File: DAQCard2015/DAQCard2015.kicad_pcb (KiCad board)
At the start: 4 copper layers, 160 x 160 mm, 191 parts, among them CON1 BARREL_JACK, K1 1462042-8, P1 QTH-090-01-F-D-A, P2 QTH-090-01-F-D-A, P3 miniDIL20, P4 LEMO_EPY.00.250.NTN, P5 LEMO_EPY.00.250.NTN, P6 FAN, P7 CONN_02X20_Double, P9 SHV, Q1 MMBT2222A-TP, Q2 SBC817-40LT1G, SW1 DPDT, U1 RJ45x8, U10 AD9219, U11 THS4524IDBTR, U12 AD9219, U13 THS4524IDBTR, U14 AD9219, U15 THS4524IDBTR, U16 AD9219, U17 THS4524IDBTR, U18 AD9219, U19 AD8534, U2 AD5628, U20 LM1086, U21 LT1913, U22 AD5628, U23 AD8534, U24 MCP65R41, U3 THS4524IDBTR, U4 AD9219, U5 THS4524IDBTR, U6 AD9219, U7 THS4524IDBTR, U8 AD9219, U9 THS4524IDBTR

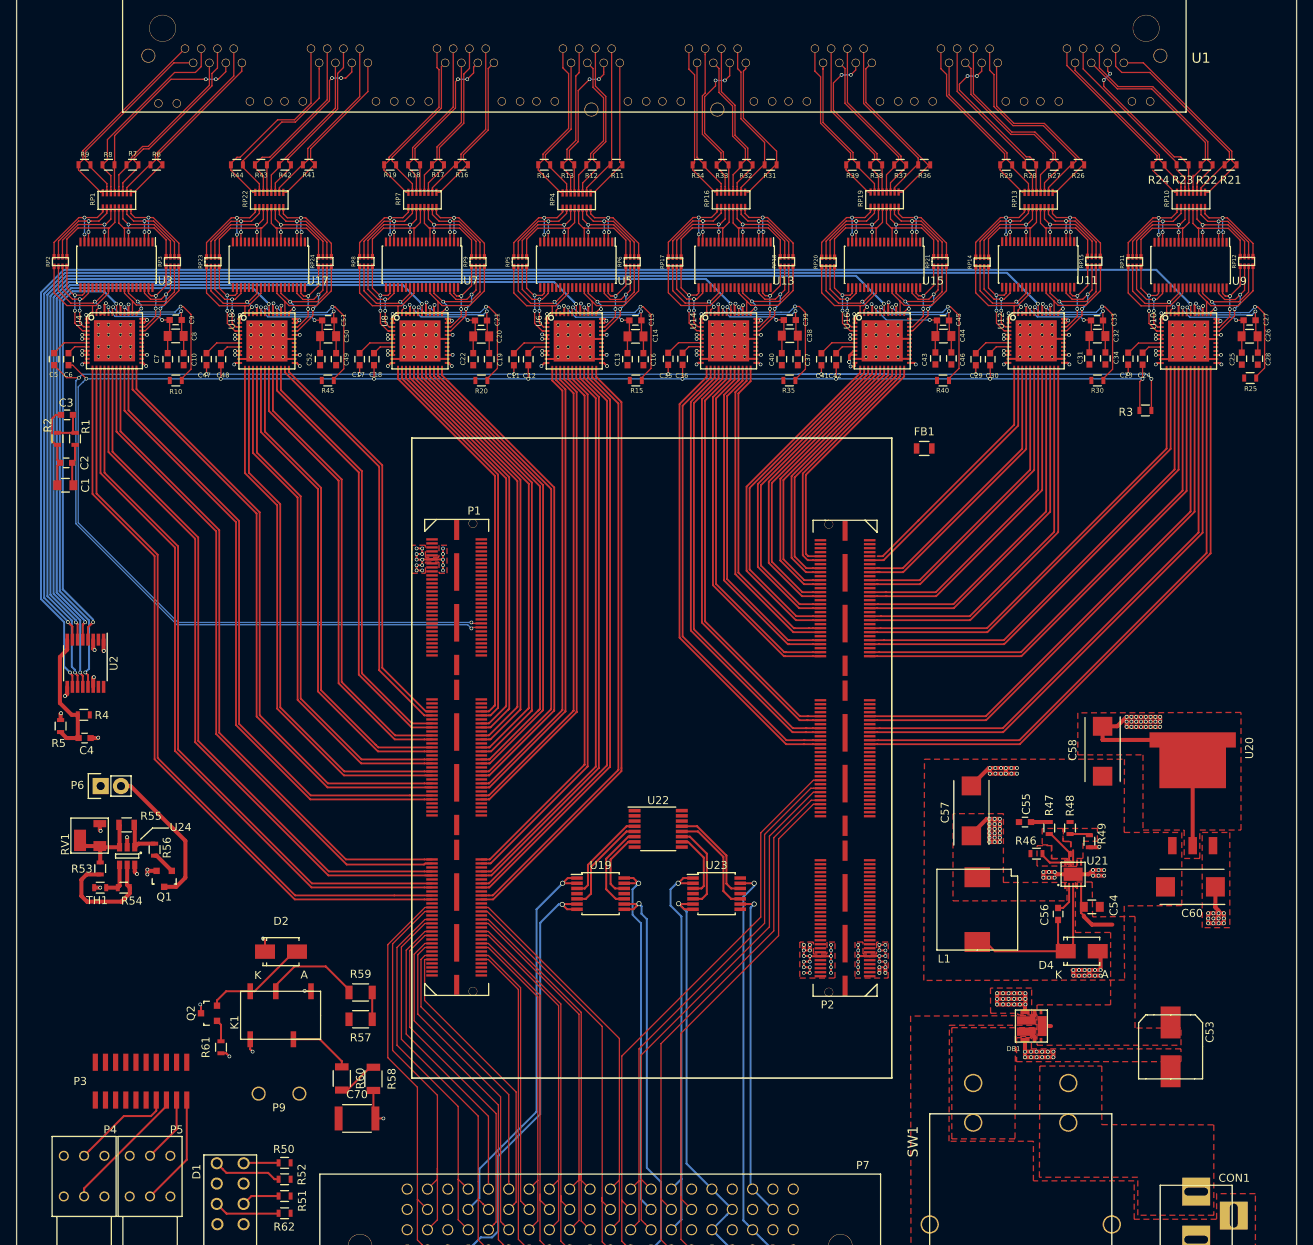
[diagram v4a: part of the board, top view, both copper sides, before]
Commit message: Adds misc traces(gnds, SPI, etc) to DAQ board
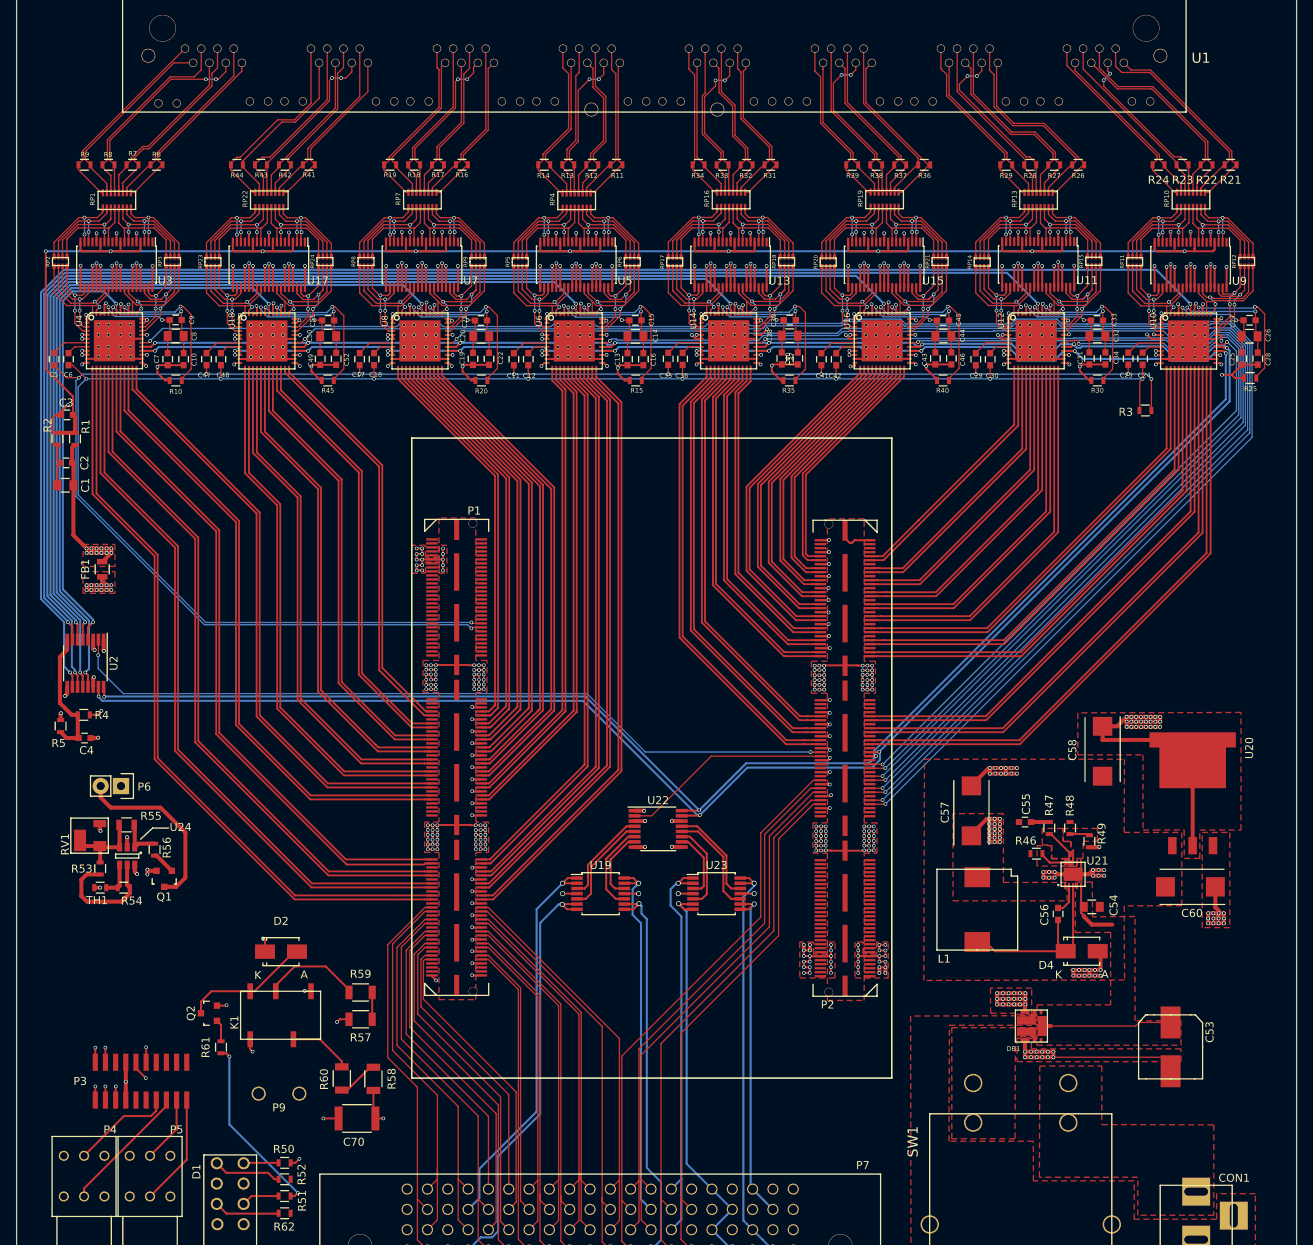
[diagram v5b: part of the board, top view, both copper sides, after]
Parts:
- moved FB1 103.9 mm to (28.7, 96.2), turned to 90 degrees
- moved P6 2.54 mm to (31.1, 123.3), turned to 180 degrees
- moved C19 2.03 mm to (75.0, 69.9)
- moved C52 2.01 mm to (58.0, 69.9)
- moved C37 2.00 mm to (113.7, 69.8)
- moved C40 2.00 mm to (115.7, 69.8)
- moved C49 1.99 mm to (56.0, 69.9)
- moved C22 1.97 mm to (77.0, 69.9)
- moved U13 0.50 mm to (107.2, 58.1)
- turned C20 to 0 degrees
- turned C21 to 180 degrees
- turned C27 to 180 degrees
- turned C38 to 0 degrees
- turned C39 to 180 degrees
- turned C50 to 0 degrees
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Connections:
- P1 pad 102: /ZEM4310/+12VDD -> (no net)
- P1 pad 108: /ZEM4310/+12VDD -> (no net)
- P1 pad 114: /ZEM4310/+12VDD -> (no net)
- P1 pad 115: /ZEM4310/CLKOUT1p -> (no net)
- P1 pad 116: /ZEM4310/CLKIN1p -> (no net)
- P1 pad 117: /ZEM4310/CLKOUT1n -> (no net)
- P1 pad 118: /ZEM4310/CLKIN1n -> (no net)
- P1 pad 120: /ZEM4310/+12VDD -> (no net)
- P1 pad 126: /ZEM4310/+12VDD -> (no net)
- P1 pad 132: /ZEM4310/+12VDD -> (no net)
- P1 pad 138: /ZEM4310/+12VDD -> (no net)
- P1 pad 144: /ZEM4310/+12VDD -> (no net)
- P1 pad 150: /ZEM4310/+12VDD -> (no net)
- P1 pad 156: /ZEM4310/+12VDD -> (no net)
- P1 pad 162: /ZEM4310/+12VDD -> (no net)
- P1 pad 168: /ZEM4310/+12VDD -> (no net)
- P1 pad 174: /ZEM4310/+12VDD -> (no net)
- P1 pad 175: /ZEM4310/CKLOUT2p -> (no net)
- P1 pad 176: /ZEM4310/CLKIN2p -> (no net)
- P1 pad 177: /ZEM4310/CKLOUT2n -> (no net)
- P1 pad 178: /ZEM4310/CLKIN2n -> (no net)
- P1 pad 49: /ZEM4310/HSMC_SDA -> (no net)
- P1 pad 50: /ZEM4310/HSMC_SCL -> (no net)
- P1 pad 51: /ZEM4310/JTAG_TCK -> (no net)
- P1 pad 52: /ZEM4310/JTAG_TMC -> (no net)
- P1 pad 55: /ZEM4310/JTAG_TDO -> (no net)
- P1 pad 56: /ZEM4310/JTAG_TDI -> (no net)
- P1 pad 57: /ZEM4310/CLKOUT0 -> (no net)
- P1 pad 58: /ZEM4310/CLKIN0 -> (no net)
- P1 pad 61: /ZEM4310/D0 -> (no net)
- P1 pad 62: /ZEM4310/D1 -> (no net)
- P1 pad 63: /ZEM4310/D2 -> (no net)
- P1 pad 64: /ZEM4310/D3 -> (no net)
- P1 pad 66: /ZEM4310/+12VDD -> (no net)
- P1 pad 72: /ZEM4310/+12VDD -> (no net)
- P1 pad 78: /ZEM4310/+12VDD -> (no net)
- P1 pad 84: /ZEM4310/+12VDD -> (no net)
- P1 pad 90: /ZEM4310/+12VDD -> (no net)
- P1 pad 96: /ZEM4310/+12VDD -> (no net)
- P2 pad 102: /ZEM4310/+12VDD -> (no net)
- P2 pad 108: /ZEM4310/+12VDD -> (no net)
- P2 pad 114: /ZEM4310/+12VDD -> (no net)
- P2 pad 115: /ZEM4310/CLKOUT1p -> (no net)
- P2 pad 116: /ZEM4310/CLKIN1p -> (no net)
- P2 pad 117: /ZEM4310/CLKOUT1n -> (no net)
- P2 pad 118: /ZEM4310/CLKIN1n -> (no net)
- P2 pad 120: /ZEM4310/+12VDD -> (no net)
- P2 pad 126: /ZEM4310/+12VDD -> (no net)
- P2 pad 132: /ZEM4310/+12VDD -> (no net)
- P2 pad 138: /ZEM4310/+12VDD -> (no net)
- P2 pad 144: /ZEM4310/+12VDD -> (no net)
- P2 pad 150: /ZEM4310/+12VDD -> (no net)
- P2 pad 156: /ZEM4310/+12VDD -> (no net)
- P2 pad 162: /ZEM4310/+12VDD -> (no net)
- P2 pad 168: /ZEM4310/+12VDD -> (no net)
- P2 pad 174: /ZEM4310/+12VDD -> (no net)
- P2 pad 175: /ZEM4310/CKLOUT2p -> (no net)
- P2 pad 176: /ZEM4310/CLKIN2p -> (no net)
- P2 pad 177: /ZEM4310/CKLOUT2n -> (no net)
- P2 pad 178: /ZEM4310/CLKIN2n -> (no net)
- P2 pad 49: /ZEM4310/HSMC_SDA -> (no net)
- P2 pad 50: /ZEM4310/HSMC_SCL -> (no net)
- P2 pad 51: /ZEM4310/JTAG_TCK -> (no net)
- P2 pad 52: /ZEM4310/JTAG_TMC -> (no net)
- P2 pad 55: /ZEM4310/JTAG_TDO -> (no net)
- P2 pad 56: /ZEM4310/JTAG_TDI -> (no net)
- P2 pad 57: /ZEM4310/CLKOUT0 -> (no net)
- P2 pad 58: /ZEM4310/CLKIN0 -> (no net)
- P2 pad 61: /ZEM4310/D0 -> (no net)
- P2 pad 62: /ZEM4310/D1 -> (no net)
- P2 pad 63: /ZEM4310/D2 -> (no net)
- P2 pad 64: /ZEM4310/D3 -> (no net)
- P2 pad 66: /ZEM4310/+12VDD -> (no net)
- P2 pad 68: (no net) -> ADC1_CSB
- P2 pad 70: (no net) -> ADC2_CSB
- P2 pad 72: /ZEM4310/+12VDD -> (no net)
- P2 pad 74: (no net) -> ADC3_CSB
- P2 pad 76: (no net) -> ADC4_CSB
- P2 pad 78: /ZEM4310/+12VDD -> (no net)
- P2 pad 80: (no net) -> ADC5_CSB
- P2 pad 82: (no net) -> ADC6_CSB
- P2 pad 84: /ZEM4310/+12VDD -> (no net)
- P2 pad 86: (no net) -> ADC7_CSB
- P2 pad 88: (no net) -> ADC8_CSB
- P2 pad 90: /ZEM4310/+12VDD -> (no net)
- P2 pad 91: (no net) -> SUPDAC_CSB
- P2 pad 92: (no net) -> SPI_SCLK
- P2 pad 93: (no net) -> RNGDAC_CSB
- P2 pad 94: (no net) -> SPI_SDIO
- P2 pad 96: /ZEM4310/+12VDD -> (no net)
- U10 pad 30: (no net) -> ADC8_CSB
- U12 pad 30: (no net) -> ADC7_CSB
- U14 pad 30: (no net) -> ADC5_CSB
- U16 pad 30: (no net) -> ADC6_CSB
- U18 pad 30: (no net) -> ADC2_CSB
- U2 pad 2: (no net) -> RNGDAC_CSB
- U22 pad 15: (no net) -> SPI_SDIO
- U22 pad 16: (no net) -> SPI_SCLK
- U22 pad 2: (no net) -> SUPDAC_CSB
- U4 pad 30: (no net) -> ADC1_CSB
- U6 pad 30: (no net) -> ADC4_CSB
- U8 pad 30: (no net) -> ADC3_CSB
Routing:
- net GND: track 115.3 -> 509.6 mm, vias 76 -> 324
- net SPI_SDIO: track 0.00 -> 331.6 mm, vias 0 -> 11
- net SPI_SCLK: track 0.00 -> 329.5 mm, vias 0 -> 11
- net Vocm: track 61.8 -> 316.9 mm, vias 1 -> 10
- net ADC1_CSB: track 0.00 -> 222.1 mm, vias 0 -> 2
- net ADC2_CSB: track 0.00 -> 200.4 mm, vias 0 -> 2
- net ADC3_CSB: track 0.00 -> 178.8 mm, vias 0 -> 2
- net ADC4_CSB: track 0.00 -> 158.6 mm, vias 0 -> 2
- net ADC5_CSB: track 0.00 -> 137.1 mm, vias 0 -> 2
- net ADC6_CSB: track 0.00 -> 116.5 mm, vias 0 -> 2
- net RNGDAC_CSB: track 0.00 -> 98.2 mm, vias 0 -> 2
- net ADC7_CSB: track 0.00 -> 96.8 mm, vias 0 -> 2
- net 3V3ana: track 33.3 -> 109.6 mm, vias 4 -> 44
- net ADC8_CSB: track 0.00 -> 74.8 mm, vias 0 -> 2
- net 3V3dig: track 2.64 -> 70.7 mm, vias 2 -> 58
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- added copper zone on F.Cu, net 3V3ana
- added copper zone on POWER.Cu, net 3V3ana
- added copper zone on F.Cu, net 3V3dig
- added copper zone on POWER.Cu, net 3V3dig
